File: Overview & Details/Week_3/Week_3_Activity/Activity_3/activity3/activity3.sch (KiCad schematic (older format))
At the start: 0 parts

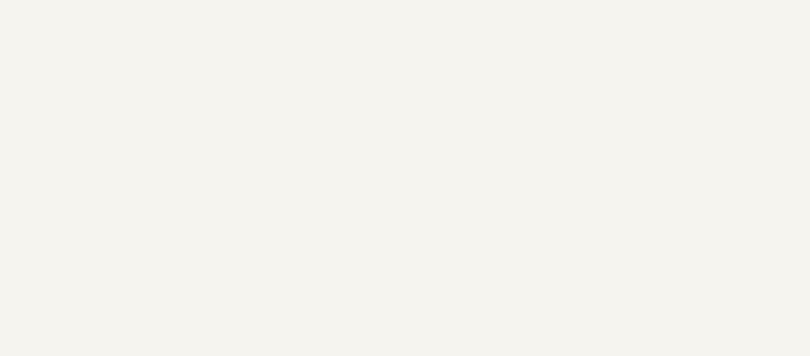
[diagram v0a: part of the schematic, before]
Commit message: made connections local to the STMPE811. removed TFT_LCD schematic. annotated schematic
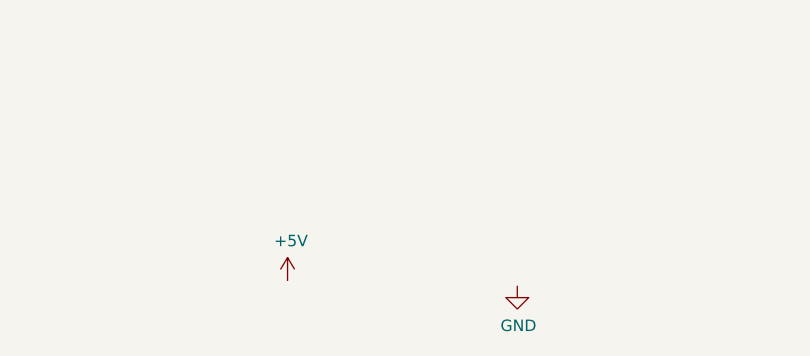
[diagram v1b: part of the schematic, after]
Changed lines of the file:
@@
 F1 "STMPE811.sch" 50
 $EndSheet
+$Comp
+L power:GND #PWR03
+U 1 1 5EE95F40
+P 6205 5120
+F 0 "#PWR03" H 6205 4870 50  0001 C CNN
+F 1 "GND" H 6210 4947 50  0000 C CNN
+F 2 "" H 6205 5120 50  0001 C CNN
+F 3 "" H 6205 5120 50  0001 C CNN
+	1    6205 5120
+	1    0    0    -1
+$EndComp
+$Comp
+L power:+5V #PWR02
+U 1 1 5EEF5BFF
+P 5200 5095
+F 0 "#PWR02" H 5200 4945 50  0001 C CNN
+F 1 "+5V" H 5215 5268 50  0000 C CNN
+F 2 "" H 5200 5095 50  0001 C CNN
+F 3 "" H 5200 5095 50  0001 C CNN
+	1    5200 5095
+	1    0    0    -1
+$EndComp
 $EndSCHEMATC

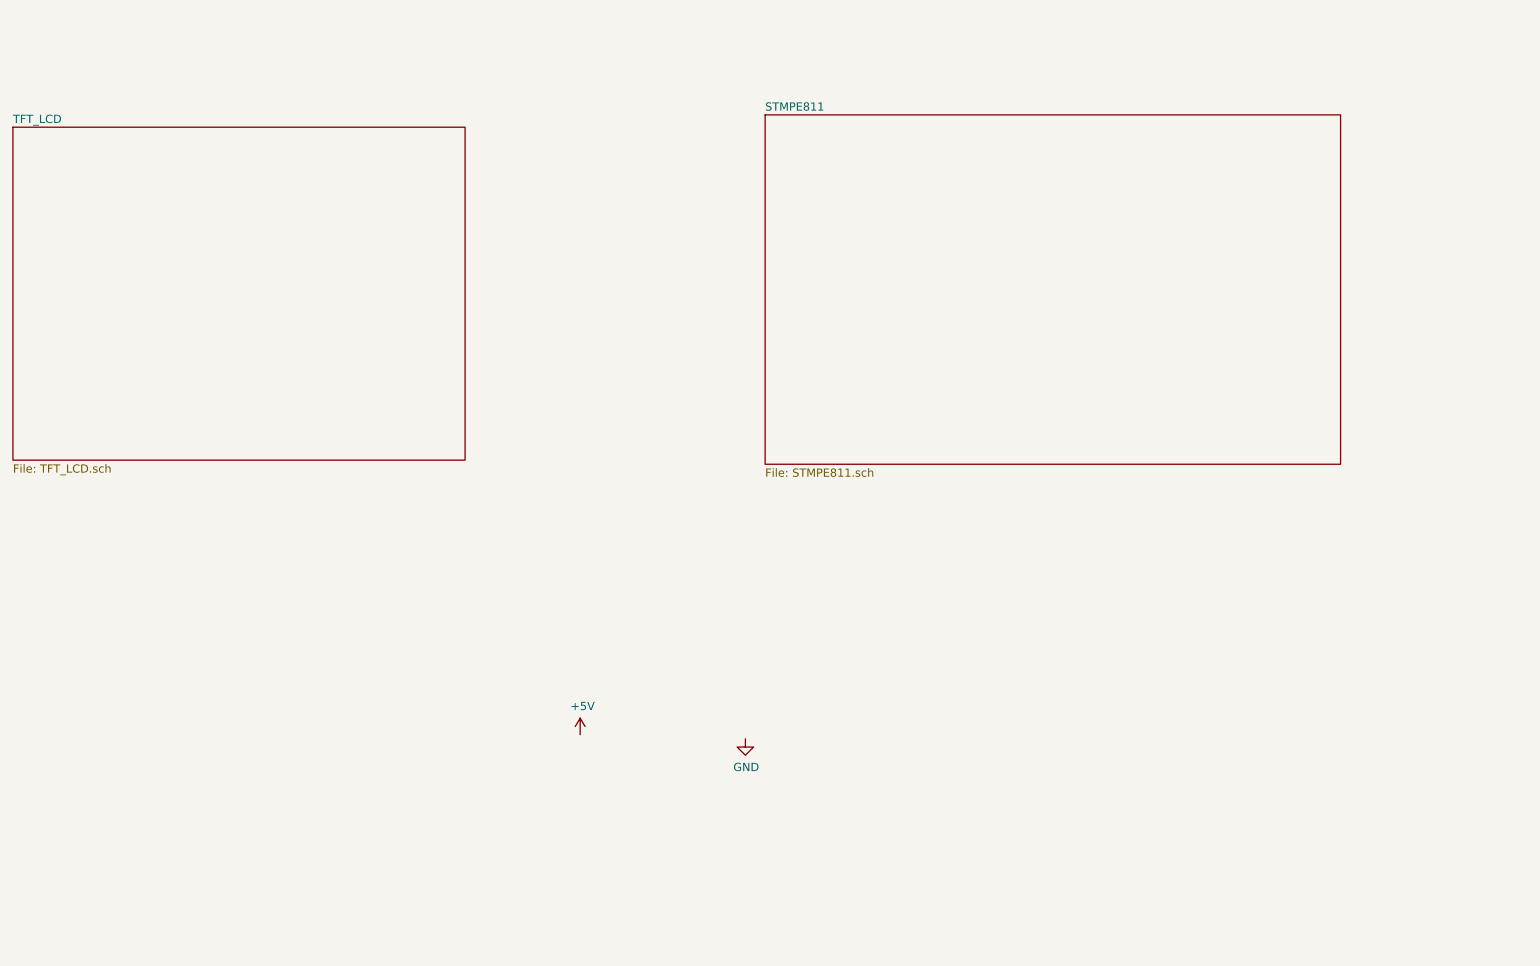
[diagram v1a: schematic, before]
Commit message: brought LED display symbol into schematic hierarchy
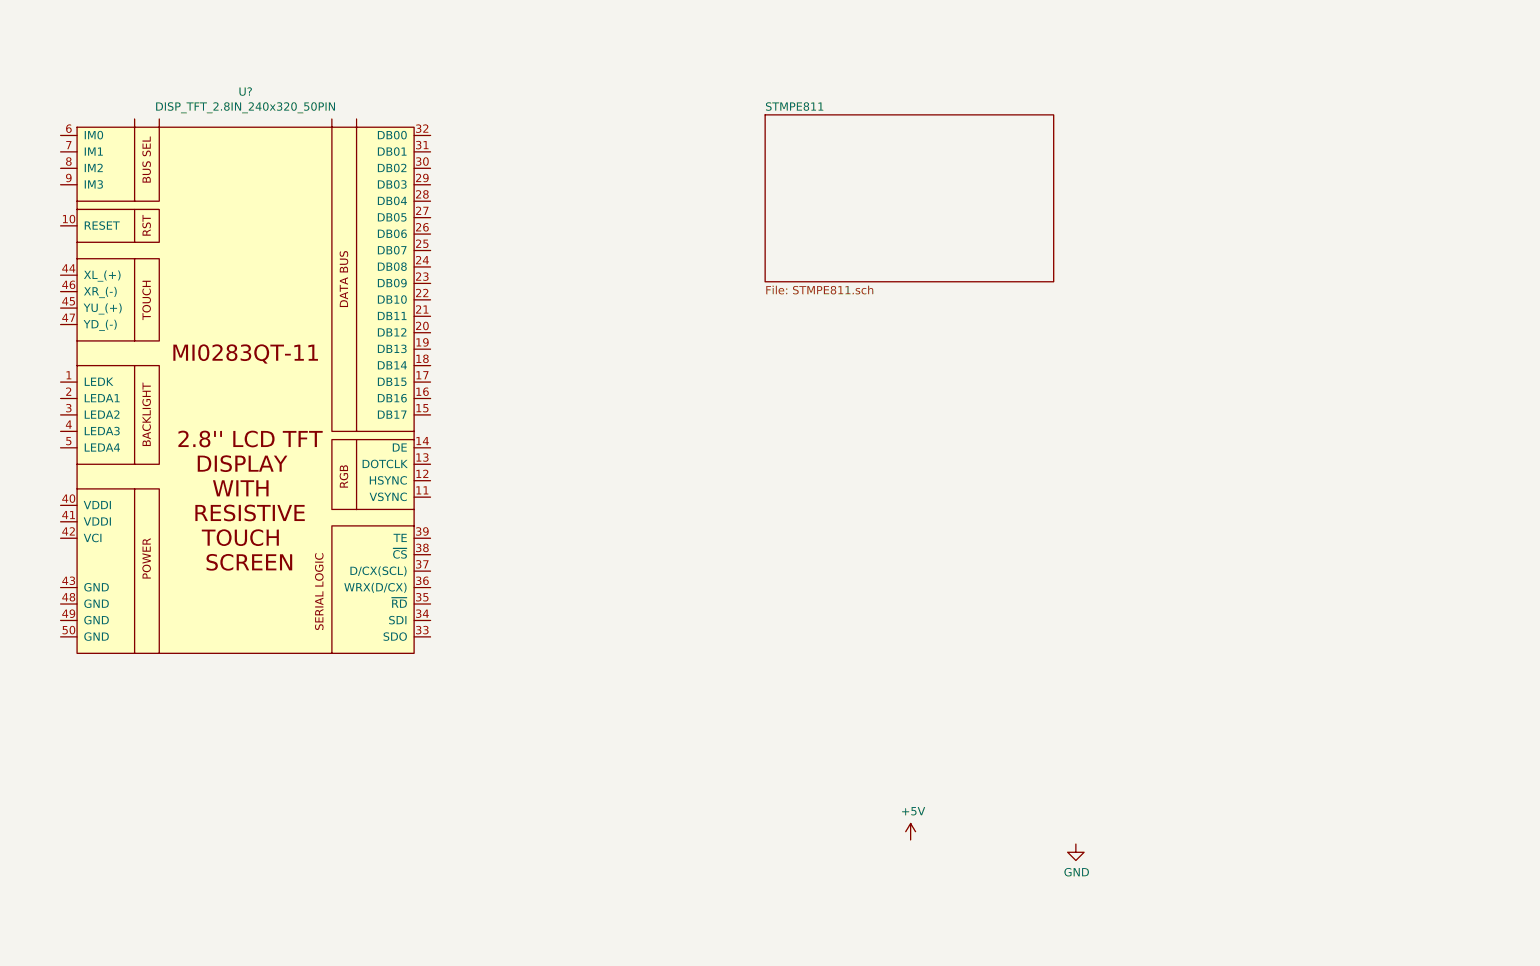
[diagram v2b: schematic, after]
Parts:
- added U?: DISP_TFT_2.8IN_240x320_50PIN, symbol Display_Board_Lib:DISP_TFT_2.8IN_240x320_50PIN
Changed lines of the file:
@@
 $Descr A4 11693 8268
 encoding utf-8
-Sheet 1 3
+Sheet 1 2
 Title ""
 Date ""
@@
 $EndDescr
 $Sheet
-S 1750 1400 2750 2025
-U 5E88F9AC
-F0 "TFT_LCD" 50
-F1 "TFT_LCD.sch" 50
-$EndSheet
-$Sheet
-S 6325 1325 3500 2125
+S 6325 1325 1755 1015
 U 5E88FA4B
 F0 "STMPE811" 50
@@
 L power:GND #PWR03
 U 1 1 5EE95F40
-P 6205 5120
-F 0 "#PWR03" H 6205 4870 50  0001 C CNN
-F 1 "GND" H 6210 4947 50  0000 C CNN
-F 2 "" H 6205 5120 50  0001 C CNN
-F 3 "" H 6205 5120 50  0001 C CNN
-	1    6205 5120
+P 8215 5760
+F 0 "#PWR03" H 8215 5510 50  0001 C CNN
+F 1 "GND" H 8220 5587 50  0000 C CNN
+F 2 "" H 8215 5760 50  0001 C CNN
+F 3 "" H 8215 5760 50  0001 C CNN
+	1    8215 5760
 	1    0    0    -1
 $EndComp
@@
 L power:+5V #PWR02
 U 1 1 5EEF5BFF
-P 5200 5095
-F 0 "#PWR02" H 5200 4945 50  0001 C CNN
-F 1 "+5V" H 5215 5268 50  0000 C CNN
-F 2 "" H 5200 5095 50  0001 C CNN
-F 3 "" H 5200 5095 50  0001 C CNN
-	1    5200 5095
+P 7210 5735
+F 0 "#PWR02" H 7210 5585 50  0001 C CNN
+F 1 "+5V" H 7225 5908 50  0000 C CNN
+F 2 "" H 7210 5735 50  0001 C CNN
+F 3 "" H 7210 5735 50  0001 C CNN
+	1    7210 5735
 	1    0    0    -1
 $EndComp
+$Comp
+L Display_Board_Lib:DISP_TFT_2.8IN_240x320_50PIN U?
+U 1 1 5F053F83
+P 3190 2900
+F 0 "U?" H 3165 4615 50  0000 C CNN
+F 1 "DISP_TFT_2.8IN_240x320_50PIN" H 3165 4524 50  0000 C CNN
+F 2 "" H 3340 2900 50  0001 C CNN
+F 3 "" H 3340 2900 50  0001 C CNN
+	1    3190 2900
+	1    0    0    -1
+$EndComp

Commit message: added 50 position FFC connector. assigned nets b/t FFC connector and display board
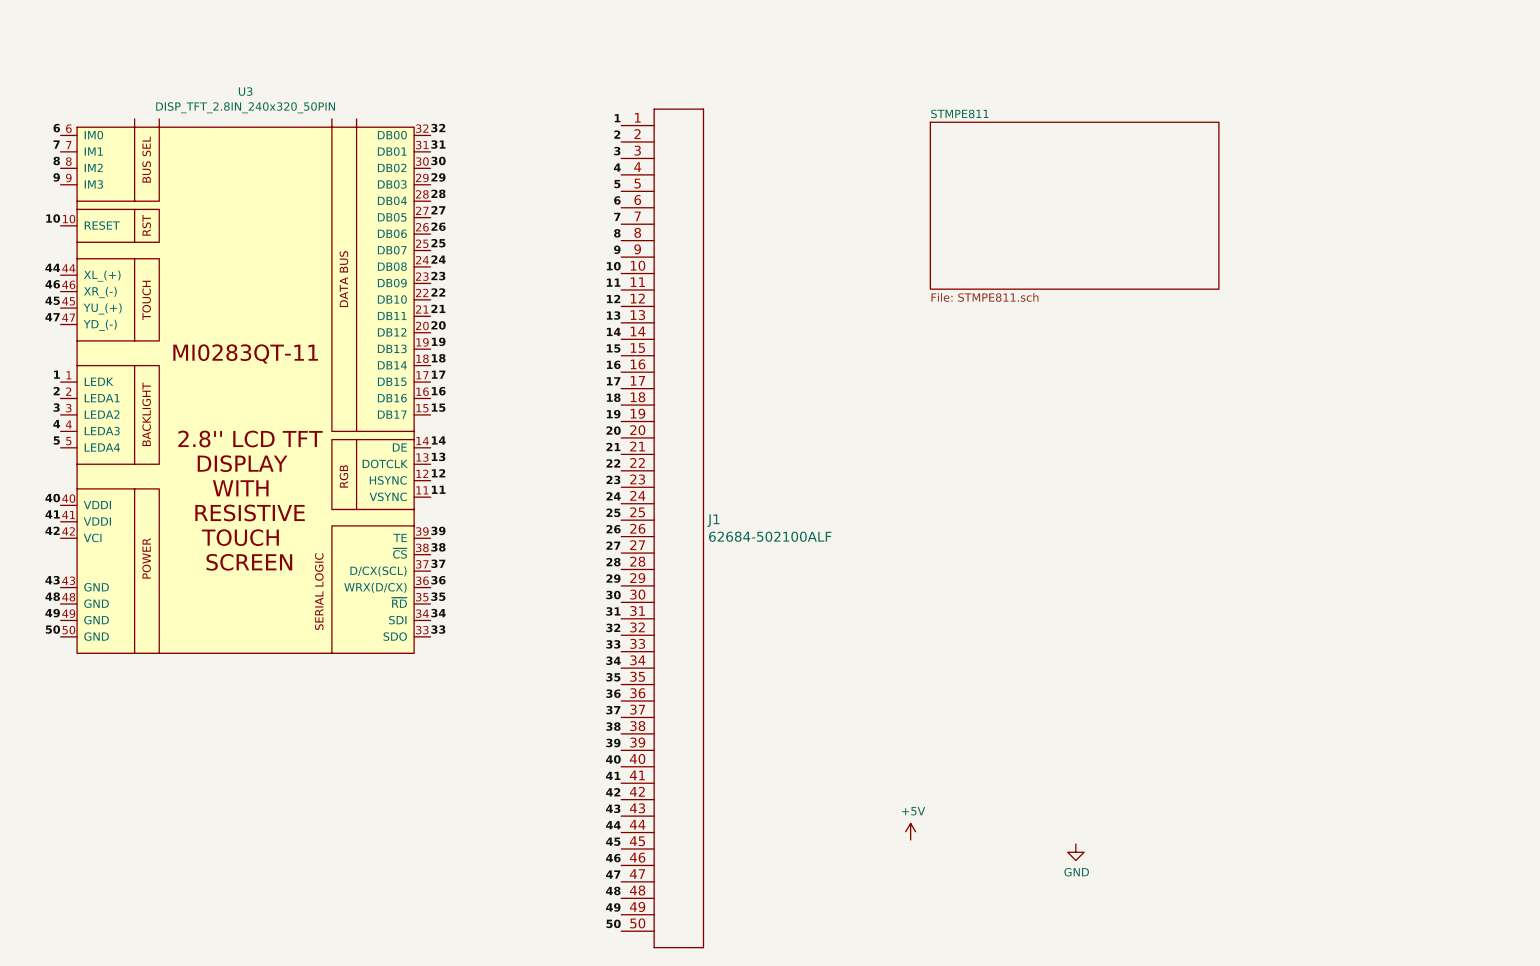
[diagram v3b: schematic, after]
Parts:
- added J1: 62684-502100ALF, CONN50_62684-502100ALF, symbol 2020-04-05_01-22-35:62684-502100ALF
- gave numbers to parts that had none: 1
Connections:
- net 1: now reaches U3.1 (LEDK)
- net 1: now also J1.1 (IN1)
- net 10: now reaches U3.10 (RESET)
- net 10: now also J1.10 (IN10)
- net 11: now reaches U3.11 (VSYNC)
- net 11: now also J1.11 (IN11)
- net 12: now reaches U3.12 (HSYNC)
- net 12: now also J1.12 (IN12)
- net 13: now reaches U3.13 (DOTCLK)
- net 13: now also J1.13 (IN13)
- net 14: now reaches U3.14 (DE)
- net 14: now also J1.14 (IN14)
- net 15: now reaches U3.15 (DB17)
- net 15: now also J1.15 (IN15)
- net 16: now reaches U3.16 (DB16)
- net 16: now also J1.16 (IN16)
- net 17: now reaches U3.17 (DB15)
- net 17: now also J1.17 (IN17)
- net 18: now reaches U3.18 (DB14)
- net 18: now also J1.18 (IN18)
- net 19: now reaches U3.19 (DB13)
- net 19: now also J1.19 (IN19)
- net 2: now reaches U3.2 (LEDA1)
- net 2: now also J1.2 (IN2)
- net 20: now reaches U3.20 (DB12)
- net 20: now also J1.20 (IN20)
- net 21: now reaches U3.21 (DB11)
- net 21: now also J1.21 (IN21)
- net 22: now reaches U3.22 (DB10)
- net 22: now also J1.22 (IN22)
- net 23: now reaches U3.23 (DB09)
- net 23: now also J1.23 (IN23)
- net 24: now reaches U3.24 (DB08)
- net 24: now also J1.24 (IN24)
- net 25: now reaches U3.25 (DB07)
- net 25: now also J1.25 (IN25)
- net 26: now reaches U3.26 (DB06)
- net 26: now also J1.26 (IN26)
- net 27: now reaches U3.27 (DB05)
- net 27: now also J1.27 (IN27)
- net 28: now reaches U3.28 (DB04)
- net 28: now also J1.28 (IN28)
- net 29: now reaches U3.29 (DB03)
- net 29: now also J1.29 (IN29)
- net 3: now reaches U3.3 (LEDA2)
- net 3: now also J1.3 (IN3)
- net 30: now reaches U3.30 (DB02)
- net 30: now also J1.30 (IN30)
- net 31: now reaches U3.31 (DB01)
- net 31: now also J1.31 (IN31)
- net 32: now reaches U3.32 (DB00)
- net 32: now also J1.32 (IN32)
- net 33: now reaches U3.33 (SDO)
- net 33: now also J1.33 (IN33)
- net 34: now reaches U3.34 (SDI)
- net 34: now also J1.34 (IN34)
- net 35: now reaches U3.35 (~RD)
- net 35: now also J1.35 (IN35)
- net 36: now reaches U3.36 (WRX(D/CX))
- net 36: now also J1.36 (IN36)
- net 37: now reaches U3.37 (D/CX(SCL))
- net 37: now also J1.37 (IN37)
- net 38: now reaches U3.38 (~CS)
- net 38: now also J1.38 (IN38)
- net 39: now reaches U3.39 (TE)
- net 39: now also J1.39 (IN39)
- net 4: now reaches U3.4 (LEDA3)
- net 4: now also J1.4 (IN4)
- net 40: now reaches U3.40 (VDDI)
- net 40: now also J1.40 (IN40)
- net 41: now reaches U3.41 (VDDI)
- net 41: now also J1.41 (IN41)
- net 42: now reaches U3.42 (VCI)
- net 42: now also J1.42 (IN42)
- net 43: now reaches U3.43 (GND)
- net 43: now also J1.43 (IN43)
- net 44: now reaches U3.44 (XL_(+))
- net 44: now also J1.44 (IN44)
- net 45: now reaches U3.45 (YU_(+))
- net 45: now also J1.45 (IN45)
- net 46: now reaches U3.46 (XR_(-))
- net 46: now also J1.46 (IN46)
- net 47: now reaches U3.47 (YD_(-))
- net 47: now also J1.47 (IN47)
- net 48: now reaches U3.48 (GND)
- net 48: now also J1.48 (IN48)
- net 49: now reaches U3.49 (GND)
- net 49: now also J1.49 (IN49)
- net 5: now reaches U3.5 (LEDA4)
- net 5: now also J1.5 (IN5)
- net 50: now reaches U3.50 (GND)
- net 50: now also J1.50 (IN50)
- net 6: now reaches U3.6 (IM0)
- net 6: now also J1.6 (IN6)
- net 7: now reaches U3.7 (IM1)
- net 7: now also J1.7 (IN7)
- net 8: now reaches U3.8 (IM2)
- net 8: now also J1.8 (IN8)
- net 9: now reaches U3.9 (IM3)
- net 9: now also J1.9 (IN9)
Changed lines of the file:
@@
 $EndDescr
 $Sheet
-S 6325 1325 1755 1015
+S 7330 1370 1755 1015
 U 5E88FA4B
 F0 "STMPE811" 50
@@
 $EndComp
 $Comp
-L Display_Board_Lib:DISP_TFT_2.8IN_240x320_50PIN U?
+L 2020-04-05_01-22-35:62684-502100ALF J1
+U 1 1 5F061D23
+P 5450 1390
+F 0 "J1" H 5978 -1007 60  0000 L CNN
+F 1 "62684-502100ALF" H 5978 -1113 60  0000 L CNN
+F 2 "CONN50_62684-502100ALF" H 5850 -1070 60  0001 C CNN
+F 3 "" H 5450 1390 60  0000 C CNN
+	1    5450 1390
+	1    0    0    -1
+$EndComp
+Text Label 4290 1450 0    50   ~ 10
+32
+Text Label 4290 1550 0    50   ~ 10
+31
+Text Label 4290 1650 0    50   ~ 10
+30
+Text Label 4290 1750 0    50   ~ 10
+29
+Text Label 5450 4490 2    50   ~ 10
+32
+Text Label 5450 4390 2    50   ~ 10
+31
+Text Label 5450 4290 2    50   ~ 10
+30
+Text Label 5450 4190 2    50   ~ 10
+29
+Text Label 4290 1850 0    50   ~ 10
+28
+Text Label 4290 1950 0    50   ~ 10
+27
+Text Label 4290 2050 0    50   ~ 10
+26
+Text Label 4290 2150 0    50   ~ 10
+25
+Text Label 4290 2250 0    50   ~ 10
+24
+Text Label 4290 2350 0    50   ~ 10
+23
+Text Label 4290 2450 0    50   ~ 10
+22
+Text Label 4290 2550 0    50   ~ 10
+21
+Text Label 4290 2650 0    50   ~ 10
+20
+Text Label 4290 2750 0    50   ~ 10
+19
+Text Label 4290 2850 0    50   ~ 10
+18
+Text Label 4290 2950 0    50   ~ 10
+17
+Text Label 4290 3050 0    50   ~ 10
+16
+Text Label 4290 3150 0    50   ~ 10
+15
+Text Label 5450 4090 2    50   ~ 10
+28
+Text Label 5450 3990 2    50   ~ 10
+27
+Text Label 5450 3890 2    50   ~ 10
+26
+Text Label 5450 3790 2    50   ~ 10
+25
+Text Label 5450 3690 2    50   ~ 10
+24
+Text Label 5450 3590 2    50   ~ 10
+23
+Text Label 5450 3490 2    50   ~ 10
+22
+Text Label 5450 3390 2    50   ~ 10
+21
+Text Label 5450 3290 2    50   ~ 10
+20
+Text Label 5450 3190 2    50   ~ 10
+19
+Text Label 5450 3090 2    50   ~ 10
+18
+Text Label 5450 2990 2    50   ~ 10
+17
+Text Label 5450 2890 2    50   ~ 10
+16
+Text Label 5450 2790 2    50   ~ 10
+15
+Text Label 4290 3350 0    50   ~ 10
+14
+Text Label 4290 3450 0    50   ~ 10
+13
+Text Label 4290 3550 0    50   ~ 10
+12
+Text Label 4290 3650 0    50   ~ 10
+11
+Text Label 5450 2690 2    50   ~ 10
+14
+Text Label 5450 2590 2    50   ~ 10
+13
+Text Label 5450 2490 2    50   ~ 10
+12
+Text Label 5450 2390 2    50   ~ 10
+11
+Text Label 4290 3900 0    50   ~ 10
+39
+Text Label 4290 4000 0    50   ~ 10
+38
+Text Label 4290 4100 0    50   ~ 10
+37
+Text Label 4290 4200 0    50   ~ 10
+36
+Text Label 4290 4300 0    50   ~ 10
+35
+Text Label 4290 4400 0    50   ~ 10
+34
+Text Label 4290 4500 0    50   ~ 10
+33
+Text Label 5450 5190 2    50   ~ 10
+39
+Text Label 5450 5090 2    50   ~ 10
+38
+Text Label 5450 4990 2    50   ~ 10
+37
+Text Label 5450 4890 2    50   ~ 10
+36
+Text Label 5450 4790 2    50   ~ 10
+35
+Text Label 5450 4690 2    50   ~ 10
+34
+Text Label 5450 4590 2    50   ~ 10
+33
+Text Label 2040 4200 2    50   ~ 10
+43
+Text Label 2040 3900 2    50   ~ 10
+42
+Text Label 2040 3800 2    50   ~ 10
+41
+Text Label 2040 3700 2    50   ~ 10
+40
+Text Label 5450 5490 2    50   ~ 10
+42
+Text Label 5450 5390 2    50   ~ 10
+41
+Text Label 5450 5290 2    50   ~ 10
+40
+Text Label 5450 5590 2    50   ~ 10
+43
+Text Label 2040 4300 2    50   ~ 10
+48
+Text Label 2040 4400 2    50   ~ 10
+49
+Text Label 2040 4500 2    50   ~ 10
+50
+$Comp
+L Display_Board_Lib:DISP_TFT_2.8IN_240x320_50PIN U3
 U 1 1 5F053F83
 P 3190 2900
-F 0 "U?" H 3165 4615 50  0000 C CNN
+F 0 "U3" H 3165 4615 50  0000 C CNN
 F 1 "DISP_TFT_2.8IN_240x320_50PIN" H 3165 4524 50  0000 C CNN
 F 2 "" H 3340 2900 50  0001 C CNN
@@
 	1    0    0    -1
 $EndComp
+Text Label 5450 6090 2    50   ~ 10
+48
+Text Label 5450 6190 2    50   ~ 10
+49
+Text Label 5450 6290 2    50   ~ 10
+50
+Text Label 2040 2950 2    50   ~ 10
+1
+Text Label 2040 3050 2    50   ~ 10
+2
+Text Label 2040 3150 2    50   ~ 10
+3
+Text Label 2040 3250 2    50   ~ 10
+4
+Text Label 2040 3350 2    50   ~ 10
+5
+Text Label 5450 1390 2    50   ~ 10
+1
+Text Label 5450 1490 2    50   ~ 10
+2
+Text Label 5450 1590 2    50   ~ 10
+3
+Text Label 5450 1690 2    50   ~ 10
+4
+Text Label 5450 1790 2    50   ~ 10
+5
+Text Label 2040 2600 2    50   ~ 10
+47
+Text Label 2040 2500 2    50   ~ 10
+45
+Text Label 2040 2400 2    50   ~ 10
+46
+Text Label 2040 2300 2    50   ~ 10
+44
+Text Label 5450 5990 2    50   ~ 10
+47
+Text Label 5450 5790 2    50   ~ 10
+45
+Text Label 5450 5890 2    50   ~ 10
+46
+Text Label 5450 5690 2    50   ~ 10
+44
+Text Label 2040 2000 2    50   ~ 10
+10
+Text Label 2040 1750 2    50   ~ 10
+9
+Text Label 2040 1650 2    50   ~ 10
+8
+Text Label 2040 1550 2    50   ~ 10
+7
+Text Label 2040 1450 2    50   ~ 10
+6
+Text Label 5450 2290 2    50   ~ 10
+10
+Text Label 5450 2190 2    50   ~ 10
+9
+Text Label 5450 2090 2    50   ~ 10
+8
+Text Label 5450 1990 2    50   ~ 10
+7
+Text Label 5450 1890 2    50   ~ 10
+6
 $EndSCHEMATC
